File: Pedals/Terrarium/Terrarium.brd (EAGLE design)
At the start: 100 x 80 mm, 32 parts, among them IC1 TL072CP, IC2 L78L05CZ, SW1 SPST, SW2 SPST, SW3 SPST, SW4 SPST, U1 ES_DAISY_SEED

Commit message: Finish base schematic
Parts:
- added IN, IN_GND, OUT, OUT_GND: PADRD, supply pins:UNLABELED
- added R1, R2, R3, R9: 1M, resistors:7.5MM.2
- added R4: 100R, resistors:7.5MM.2
- added R6: 100K, resistors:7.5MM.2
- added R7: 1K, resistors:7.5MM.2
- POT1, POT2, POT3, POT4, POT5, POT6: value (none) -> B10K
- R5, R8: value 1k -> 1K; device SparkFun-Resistors:AXIAL-0.3 -> resistors:7.5MM.2
- moved R8 171.7 mm to (-64.8, -90.2)
- moved R5 158.8 mm to (-64.8, -87.6)
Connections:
- removed net IC1_1: IC1.1
- removed net IC1_2: IC1.2
- removed net IC1_3: IC1.3
- removed net IC1_4: IC1.4
- removed net IC1_5: IC1.5
- removed net IC1_6: IC1.6
- removed net IC1_7: IC1.7
- removed net IC1_8: IC1.8
- new net N$10: C3.2, R4.1
- new net N$11: C3.1, OUT.P$1, R6.1
- new net N$12: C1.1, C6.2, IN.P$1
- new net N$14: IC1.6, IC1.7, R4.2
- new net N$15: C6.1, R7.2
- new net N$16: C7.1, IC1.3, R1.2, R3.1, R7.1
- new net N$17: C2.1, IC1.5, R2.1, R9.2
- net +5V: now also IC1.8, R1.1, R2.2
- net GND: now also C1.2, C7.2, IC1.4, IN_GND.P$1, OUT_GND.P$1, R3.2, R6.2, R9.1
- net LED1: now also R5.2; no longer R5.P$2
- net LED2: now also R8.2; no longer R8.P$2
- net LEFT_IN: now also IC1.1, IC1.2
- net LEFT_OUT: now also C2.2
- net N$7: now also R5.1; no longer R5.P$1
- net N$8: now also R8.1; no longer R8.P$1

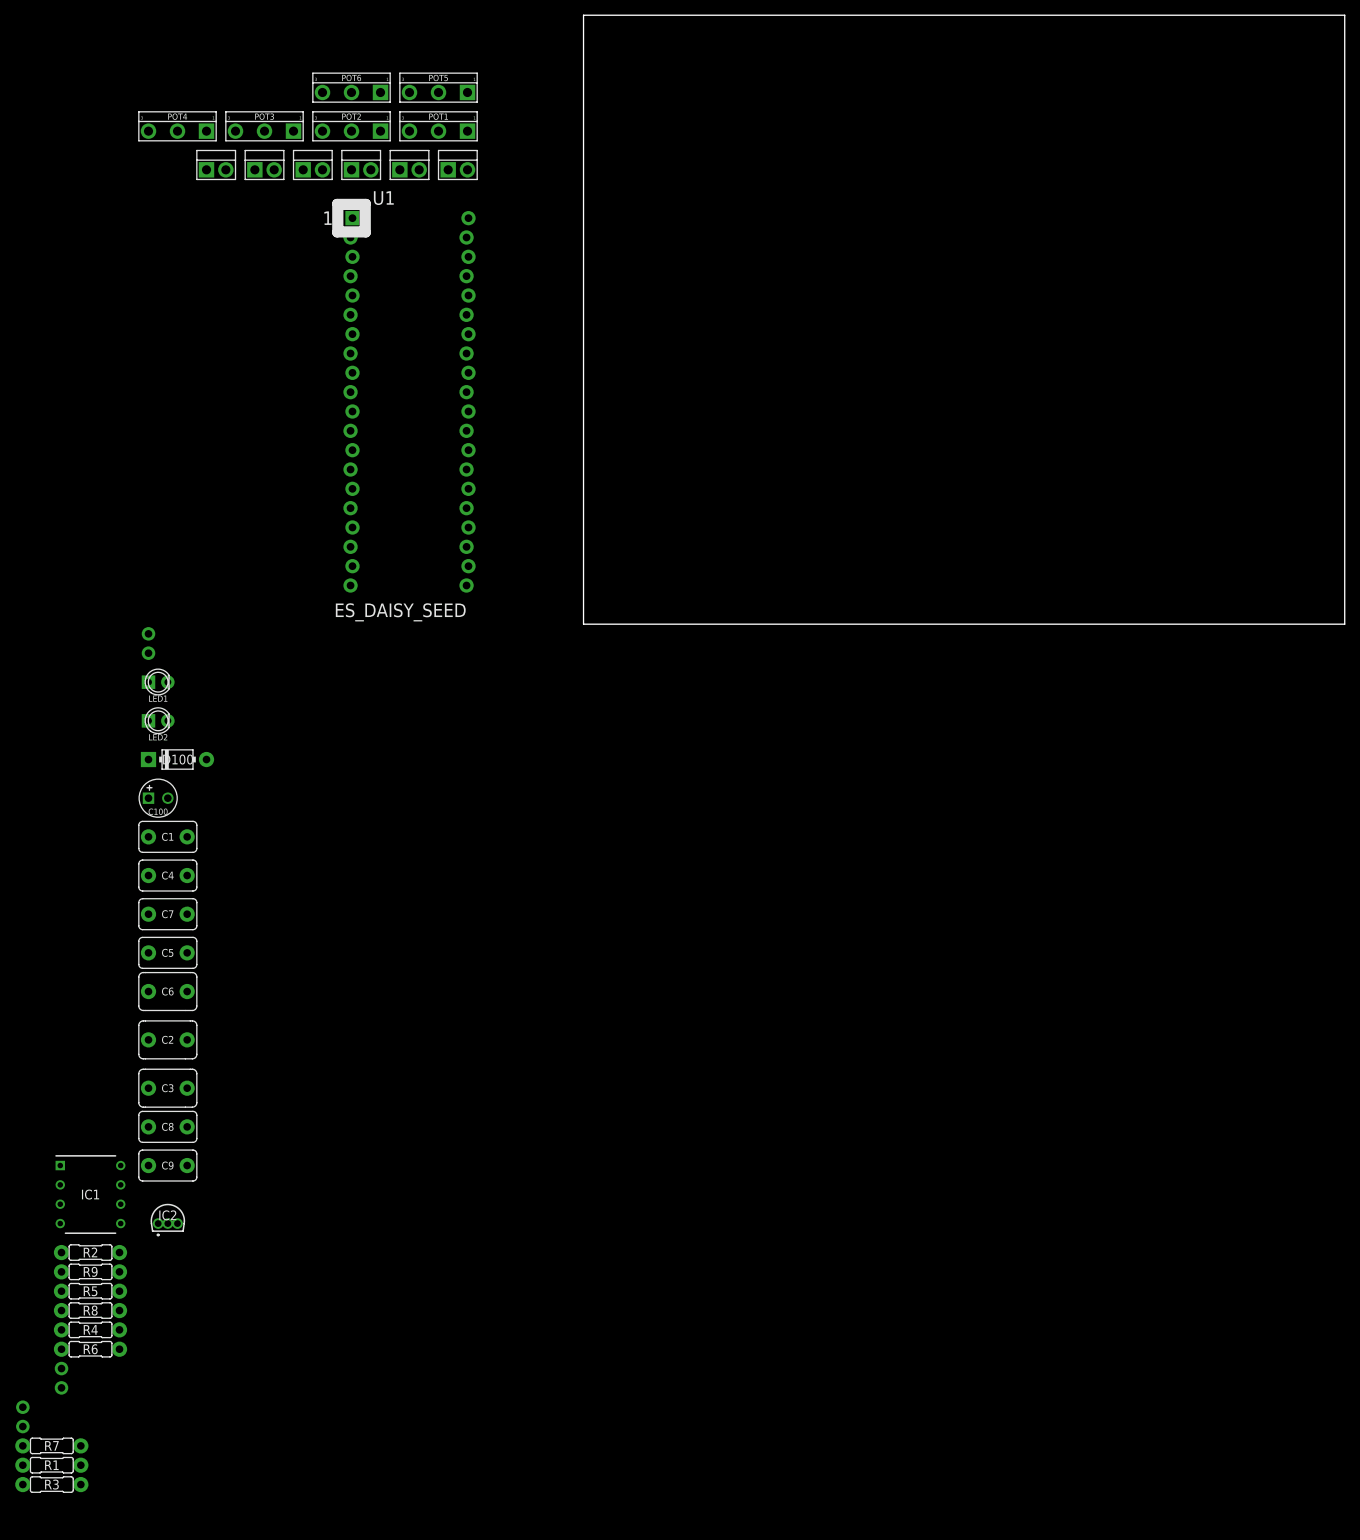
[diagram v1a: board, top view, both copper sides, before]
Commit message: Begin board layout
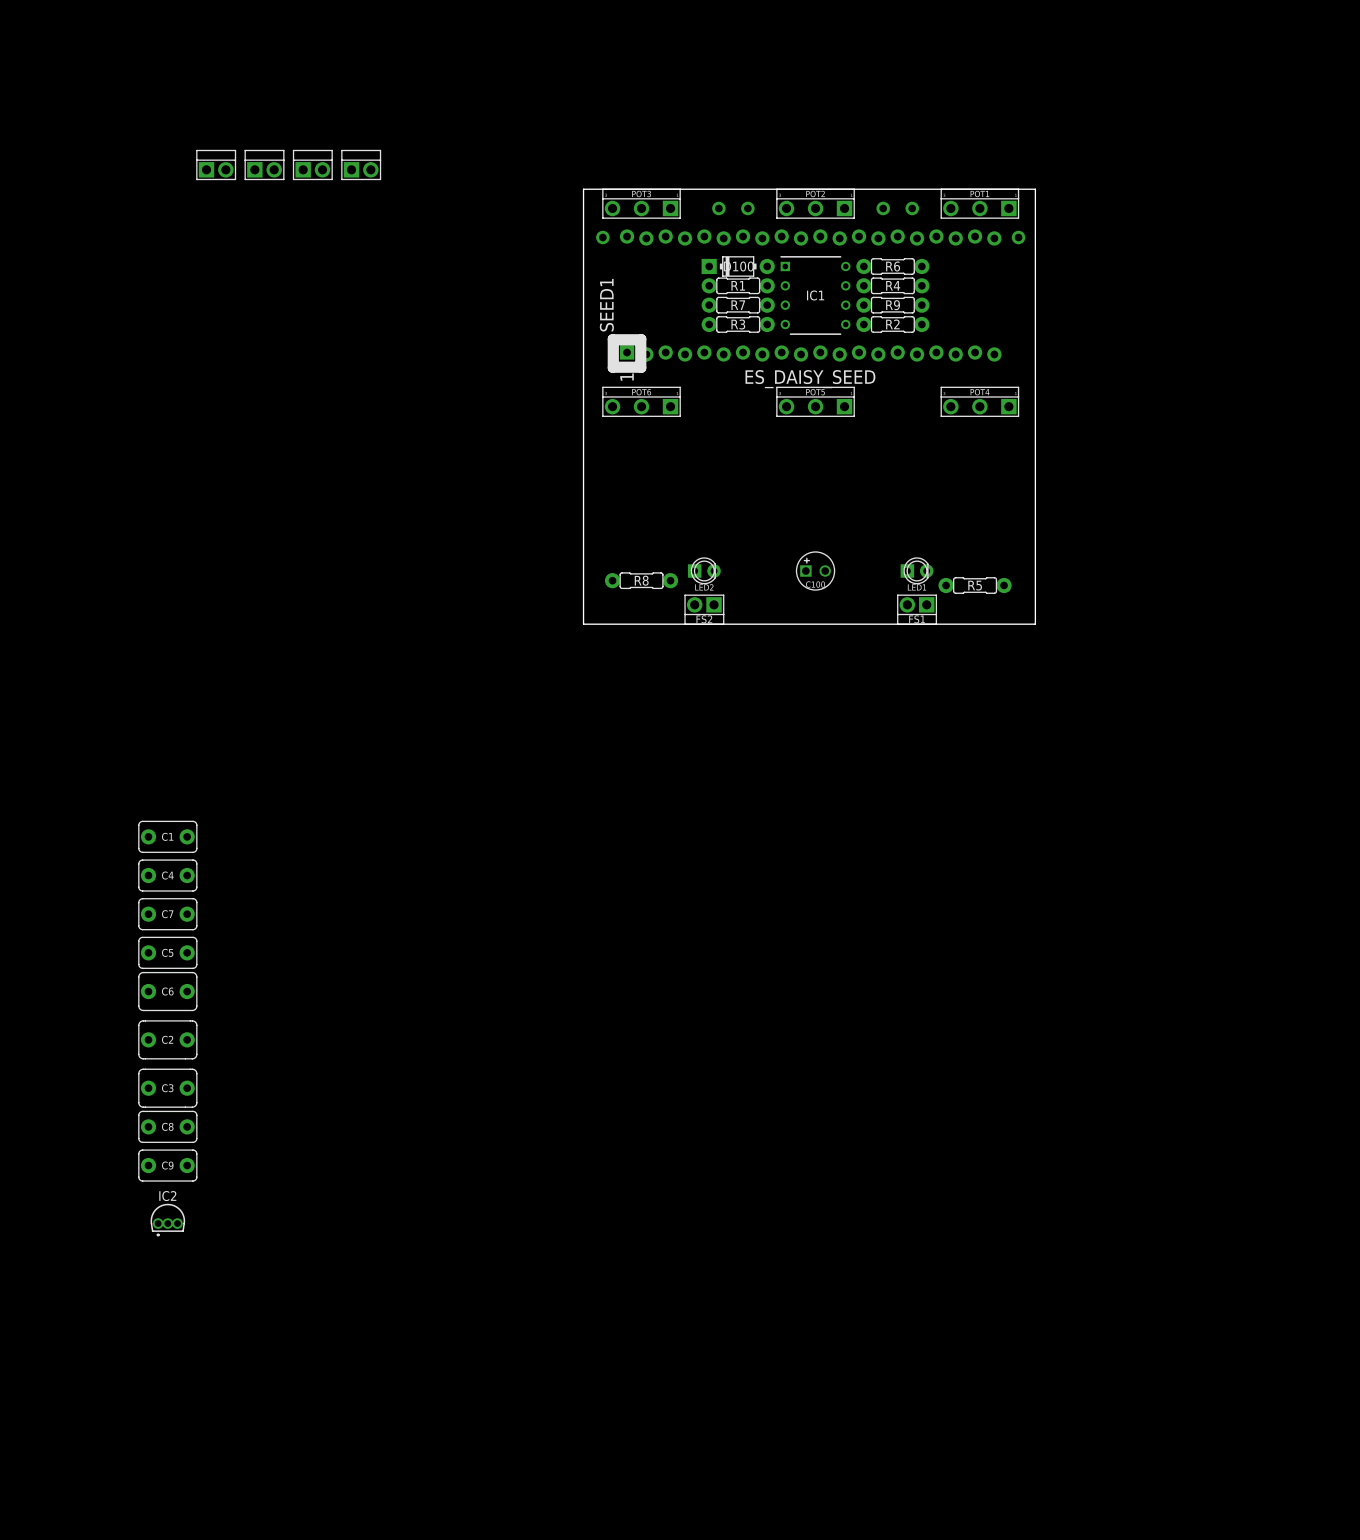
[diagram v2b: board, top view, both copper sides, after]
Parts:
- removed U1: ES_DAISY_SEED, Electrosmith_Boards:ES_DAISY_SEED
- added SEED1: ES_DAISY_SEED, Electrosmith_Boards:ES_DAISY_SEED
- moved OUT 194.6 mm to (57.1, 50.8)
- moved OUT_GND 191.0 mm to (43.2, 54.6)
- moved IN_GND 184.3 mm to (17.8, 54.6)
- moved R1 179.3 mm to (20.3, 44.5)
- moved R3 177.1 mm to (20.3, 39.4)
- moved R6 177.0 mm to (40.6, 47.0)
- moved R7 174.9 mm to (20.3, 41.9)
- moved R4 173.0 mm to (40.6, 44.5)
- moved IN 171.5 mm to (2.54, 50.8)
- moved R9 165.0 mm to (40.6, 41.9)
- moved R2 161.2 mm to (40.6, 39.4)
- moved IC1 151.7 mm to (30.5, 43.2)
- moved R5 148.7 mm to (51.4, 5.08)
- moved R8 120.1 mm to (7.62, 5.71)
- moved GND 112.8 mm to (39.4, 54.6)
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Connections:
- net 3V3_A: now also SEED1.21; no longer U1.21
- net 3V3_D: now also SEED1.38; no longer U1.38
- net FS1: now also SEED1.32; no longer U1.32
- net FS2: now also SEED1.33; no longer U1.33
- net GND: now also SEED1.20, SEED1.40; no longer U1.20, U1.40
- net LED1: now also SEED1.29; no longer U1.29
- net LED2: now also SEED1.30; no longer U1.30
- net LEFT_IN: now also SEED1.16; no longer U1.16
- net LEFT_OUT: now also SEED1.18; no longer U1.18
- net N$1: now also SEED1.23; no longer U1.23
- net N$2: now also SEED1.24; no longer U1.24
- net N$3: now also SEED1.25; no longer U1.25
- net N$4: now also SEED1.26; no longer U1.26
- net N$5: now also SEED1.27; no longer U1.27
- net N$6: now also SEED1.28; no longer U1.28
- net SW1: now also SEED1.11; no longer U1.11
- net SW2: now also SEED1.10; no longer U1.10
- net SW3: now also SEED1.9; no longer U1.9
- net SW4: now also SEED1.8; no longer U1.8
- net VCC: now also SEED1.39; no longer U1.39
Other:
- board size 100 x 80 mm -> 59.4 x 57.1 mm

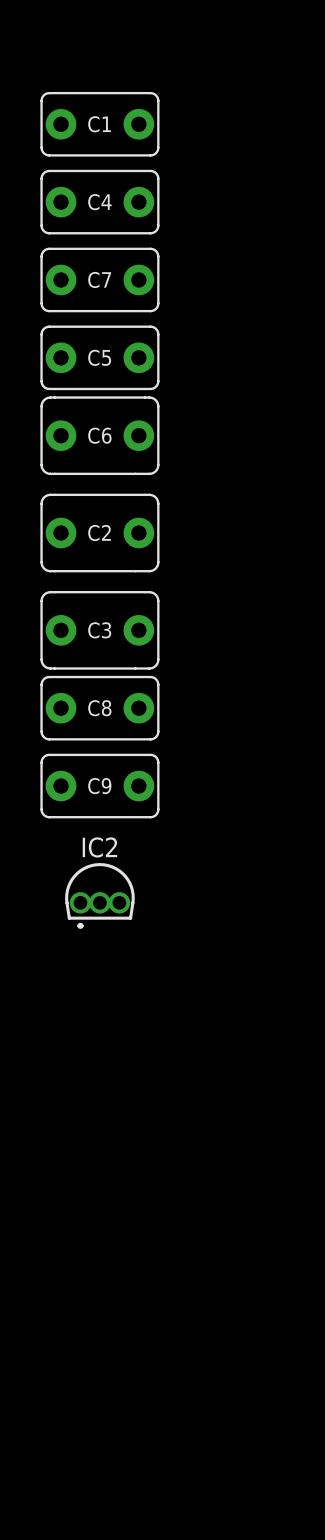
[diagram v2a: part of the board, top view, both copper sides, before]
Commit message: Fix capacitor sizes
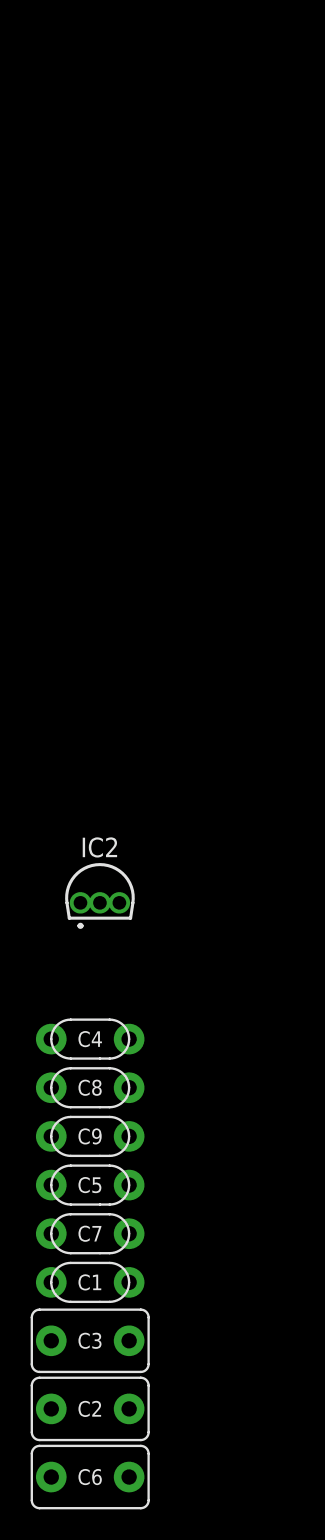
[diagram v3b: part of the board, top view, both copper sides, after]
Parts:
- C1, C4, C5, C7, C8, C9: device capacitors-film:.33UF+ -> capacitors-film:5MM
- C2, C3, C6: device capacitors-film:1UF -> capacitors-film:.33UF+
- moved C1 75.6 mm to (-55.2, -103.5)
- moved C6 67.9 mm to (-55.2, -116.2)
- moved C7 62.2 mm to (-55.2, -100.3)
- moved C2 57.2 mm to (-55.2, -111.8)
- moved C4 54.6 mm to (-55.2, -87.6)
- moved C5 54.0 mm to (-55.2, -97.2)
- moved C3 46.4 mm to (-55.2, -107.3)
- moved C8 24.8 mm to (-55.2, -90.8)
- moved C9 22.9 mm to (-55.2, -94.0)
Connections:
- net GND: now also C1.1, C7.1; no longer C1.2, C7.2
- net LEFT_OUT: now also C2.1; no longer C2.2
- net N$10: now also C3.1; no longer C3.2
- net N$11: now also C3.2; no longer C3.1
- net N$12: now also C1.2, C6.1; no longer C1.1, C6.2
- net N$15: now also C6.2; no longer C6.1
- net N$16: now also C7.2; no longer C7.1
- net N$17: now also C2.2; no longer C2.1
